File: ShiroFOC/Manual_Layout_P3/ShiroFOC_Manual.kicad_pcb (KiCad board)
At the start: 6 copper layers, 45 x 45 mm, 279 parts, among them J1 Motor phases - solder wires, J1001 TC2030-NL SWD, J101 DC input - solder wires, J201 USB-C service, J501 BRAKE RESISTOR, J502 5V PWM FAN, J601 EXT ENCODER / HALL, J801 CAN 1, J802 CAN 2, Q201 CSD17483F4, Q301 CSD17483F4, Q501 ISZ080N10NM6 100V, Q801 CSD17483F4, Q802 CSD87502Q2, SW301 RESET, U1 CSD88599Q5DC, U2 CSD88599Q5DC, U201 LMR36510FADDAR, U202 USBLC6-2SC6, U203 TPS2121RUXR, U204 TLV75533PDYDR, U205 MPM3620AGQV-Z, U3 CSD88599Q5DC, U4 STSPIN32G4, U501 UCC27517ADBVR, U502 TLV3012BIDCKR, U503 74AHCT1G125W5-7, U601 AS5047P-ATSM, U602 TMUX1574PW, U603 74LVC3G17, U604 TPS2553DBVR, U701 BMI323, U801 TCAN3413DRBR, U901 CP2102N-A02-GQFN20, Y301 24MHz 7pF

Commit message: Routing started
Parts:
- removed C107: RC DAMP C - TUNE, Capacitor_SMD:C_2220_5750Metric
- removed C125, C126, C142, C143, C159, C160: 10uF DNP, Capacitor_SMD:C_1210_3225Metric
- removed C413, C423, C433: TUNE DNP, Capacitor_SMD:C_1206_3216Metric
- removed D101: VM TVS - SELECT AFTER TEST, Diode_SMD:D_SMC
- removed R102: RC DAMP R - TUNE, Resistor_SMD:R_2512_6332Metric
- removed R303: 2k2, Resistor_SMD:R_0402_1005Metric
- removed R415, R425, R435: TUNE DNP, Resistor_SMD:R_1206_3216Metric
- removed SW301: RESET, Button_Switch_SMD:SW_Push_1P1T-SH_NO_CK_KMR2xxG
- C506, C605, C607, C701, C702, R101, R307, R308, U503, U701: moved to B.Cu
- R313, R314: moved to F.Cu
- moved C702 78.8 mm to (-3.90, -5.90)
- moved C701 78.8 mm to (-3.90, -4.02)
- moved J1001 76.4 mm to (12.1, 20.5), turned to 180 degrees
- moved U701 75.0 mm to (-6.01, -4.96)
- moved R308 73.5 mm to (-8.59, -4.71)
- moved TH701 73.3 mm to (-13.5, 36.8)
- moved R715 73.3 mm to (-8.59, -5.70)
- moved C106 70.0 mm to (11.0, -8.17), turned to 90 degrees
- moved C105 68.1 mm to (12.0, -8.17), turned to 90 degrees
- moved TH702 62.4 mm to (-14.4, 41.4)
- moved TH703 59.3 mm to (-13.1, 52.0)
- moved R101 57.3 mm to (25.3, -9.53), turned to 90 degrees
- moved C607 54.3 mm to (-1.57, 18.1), turned to 180 degrees
- moved C603 50.6 mm to (-7.27, 16.2), turned to 180 degrees
- moved C605 49.0 mm to (-13.1, 16.7), turned to 180 degrees
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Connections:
- U602 pad 4: FEEDBACK_A_H1 -> FEEDBACK_B_H2
- U602 pad 7: FEEDBACK_B_H2 -> FEEDBACK_A_H1
- U603 pad 5: Net-(U602A-S2B) -> Net-(U602A-S1B)
- U603 pad 7: Net-(U602A-S1B) -> Net-(U602A-S2B)
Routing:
- net GND: track 19.4 -> 54.5 mm, vias 12 -> 15
- net VM: track 18.1 -> 52.3 mm
- net 3V3: track 19.9 -> 36.0 mm, vias 6 -> 5
- net GLS3: track 18.8 -> 6.56 mm, vias 3 -> 2
- net Net-(R103-Pad2): track 0.00 -> 8.31 mm, vias 0 -> 2
- net GLS2: track 16.2 -> 7.98 mm
- net EXT_VCC: track 0.00 -> 8.06 mm, vias 0 -> 1
- net Net-(U601-MOSI): track 0.00 -> 7.37 mm, vias 0 -> 1
- net Net-(U602A-S1B): track 0.00 -> 5.40 mm
- net PHASE_U: track 0.00 -> 4.78 mm
- net PHASE_V: track 0.00 -> 4.30 mm
- net Net-(U602A-S2B): track 0.00 -> 4.15 mm
- net Net-(U503-A): track 0.00 -> 4.06 mm
- net SPI3_MOSI_MCU: track 0.00 -> 3.81 mm
- net GLS1: track 19.3 -> 15.7 mm
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- added copper zone on F.Cu, net /Three-phase bridge/LS_SOURCE_U
- added copper zone on F.Cu, net /Three-phase bridge/LS_SOURCE_V
- added copper zone on F.Cu, net /Three-phase bridge/LS_SOURCE_W
- added copper zone on F.Cu, net GND
- added copper zone on F.Cu, net PHASE_U
- added copper zone on F.Cu, net PHASE_V
- added copper zone on F.Cu, net PHASE_W
- added copper zone on F.Cu, net VM
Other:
- board text removed: "10 V AUXILIARY POWER"
- board text removed: "5 V / POWER MUX / 3.3 V"
- board text removed: "50 x 50 mm"
- board text removed: "55 x 55 mm"
- board text removed: "60 x 60 mm"
- board text removed: "70 x 70 mm"
- board text removed: "80 x 80 mm"
- board text removed: "BRAKE CHOPPER"
- board text removed: "BRAKE NTC"
- board text removed: "BRIDGE ROUTING - FIXED"
- board text removed: "CAN INTERFACE"
- board text removed: "DC INPUT"
- board text removed: "DC LINK / BULK CAPACITORS"
- board text removed: "DC LINK PROTECTION / DAMPING"
- board text removed: "ENCODER - CENTRED AS5047"
- board text removed: "EXTERNAL ENCODER / HALL"
- board text removed: "FEEDBACK MUX / BUS SENSE"
- board text removed: "HALF-BRIDGES / SHUNTS - FIXED"
- board text removed: "IMU"
- board text removed: "MCU + ANALOG - FIXED"
- board text removed: "MCU / OP-AMP R + C - FIXED"
- board text removed: "RESET / STATUS"
- board text removed: "SWD"
- board text removed: "TEMPERATURE / ADC FILTERS"
- board text removed: "USB / UART"

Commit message: most caps placed
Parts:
- removed C148, C150, C153, C155, C157: 10uF, Capacitor_SMD:C_1210_3225Metric
- removed R313, R314: 22R, Resistor_SMD:R_0402_1005Metric
- removed R611: 33R, Resistor_SMD:R_0402_1005Metric
- C101, C102, C103, C105, C106, C11, C110, C111, C112, C113, C114, C115, C116, C117, C118, C119, C120, C121, C123, C124, C127, C128, C129, C130, C134, C135, C136, C137, C139, C144, C145, C146, C147, C149, C154, C156, C158, C3, C7: moved to B.Cu
- C701, C702, R103, R308, R715, R903, U701: moved to F.Cu
- moved C147 100.2 mm to (5.55, 17.1), turned to 180 degrees
- moved C146 97.6 mm to (5.55, 7.40), turned to 180 degrees
- moved C156 95.8 mm to (5.55, -4.16), turned to 180 degrees
- moved C158 95.8 mm to (5.55, 4.15), turned to 180 degrees
- moved C154 93.4 mm to (10.2, -5.60), turned to 180 degrees
- moved C140 93.1 mm to (7.34, 20.0), turned to -90 degrees
- moved C130 89.3 mm to (5.55, 10.7), turned to 180 degrees
- moved C141 88.1 mm to (10.6, 20.0), turned to -90 degrees
- moved C139 87.1 mm to (6.25, 0.20), turned to 90 degrees
- moved C152 84.8 mm to (13.8, 20.0), turned to -90 degrees
- moved C151 83.4 mm to (9.81, -6.72), turned to 90 degrees
- moved C136 78.9 mm to (2.56, -8.55), turned to 180 degrees
- moved C149 77.6 mm to (15.5, -16.4), turned to -90 degrees
- moved C144 76.4 mm to (14.8, 13.9)
- moved C133 74.8 mm to (6.73, -20.0), turned to -90 degrees
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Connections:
- U601 pad 2: Net-(U601-CLK) -> SPI3_SCK_MCU
- U601 pad 3: Net-(U601-MISO) -> SPI3_MISO
- U601 pad 4: Net-(U601-MOSI) -> SPI3_MOSI_MCU
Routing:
- net VM: track 52.3 -> 99.9 mm
- net GHS2: track 19.0 -> 60.5 mm
- net FDCAN1_RX: track 0.00 -> 31.5 mm, vias 1 -> 2
- net FDCAN1_TX: track 1.35 -> 29.0 mm, vias 1 -> 2
- net USB_UART_RX: track 0.00 -> 26.5 mm, vias 1 -> 2
- net /USB service/UART_BRIDGE_RX: track 4.90 -> 30.0 mm, vias 1 -> 2
- net I2C2_SCL: track 1.16 -> 15.9 mm, vias 1 -> 2
- net SHUNT_U_SENSE_P: track 25.0 -> 10.4 mm
- net /MCU / clock / SWD/SWCLK: track 0.00 -> 13.6 mm, vias 0 -> 2
- net AS5047P_CS_N: track 0.00 -> 13.4 mm, vias 0 -> 2
- net SHUNT_U_SENSE_N: track 24.7 -> 11.4 mm
- net I2C2_SDA: track 1.16 -> 13.5 mm, vias 1 -> 2
- net SPI3_MISO: track 0.00 -> 10.9 mm, vias 0 -> 1
- net GND: track 54.5 -> 65.0 mm, vias 15 -> 13
- net HS_RETURN_U: track 21.0 -> 10.8 mm
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
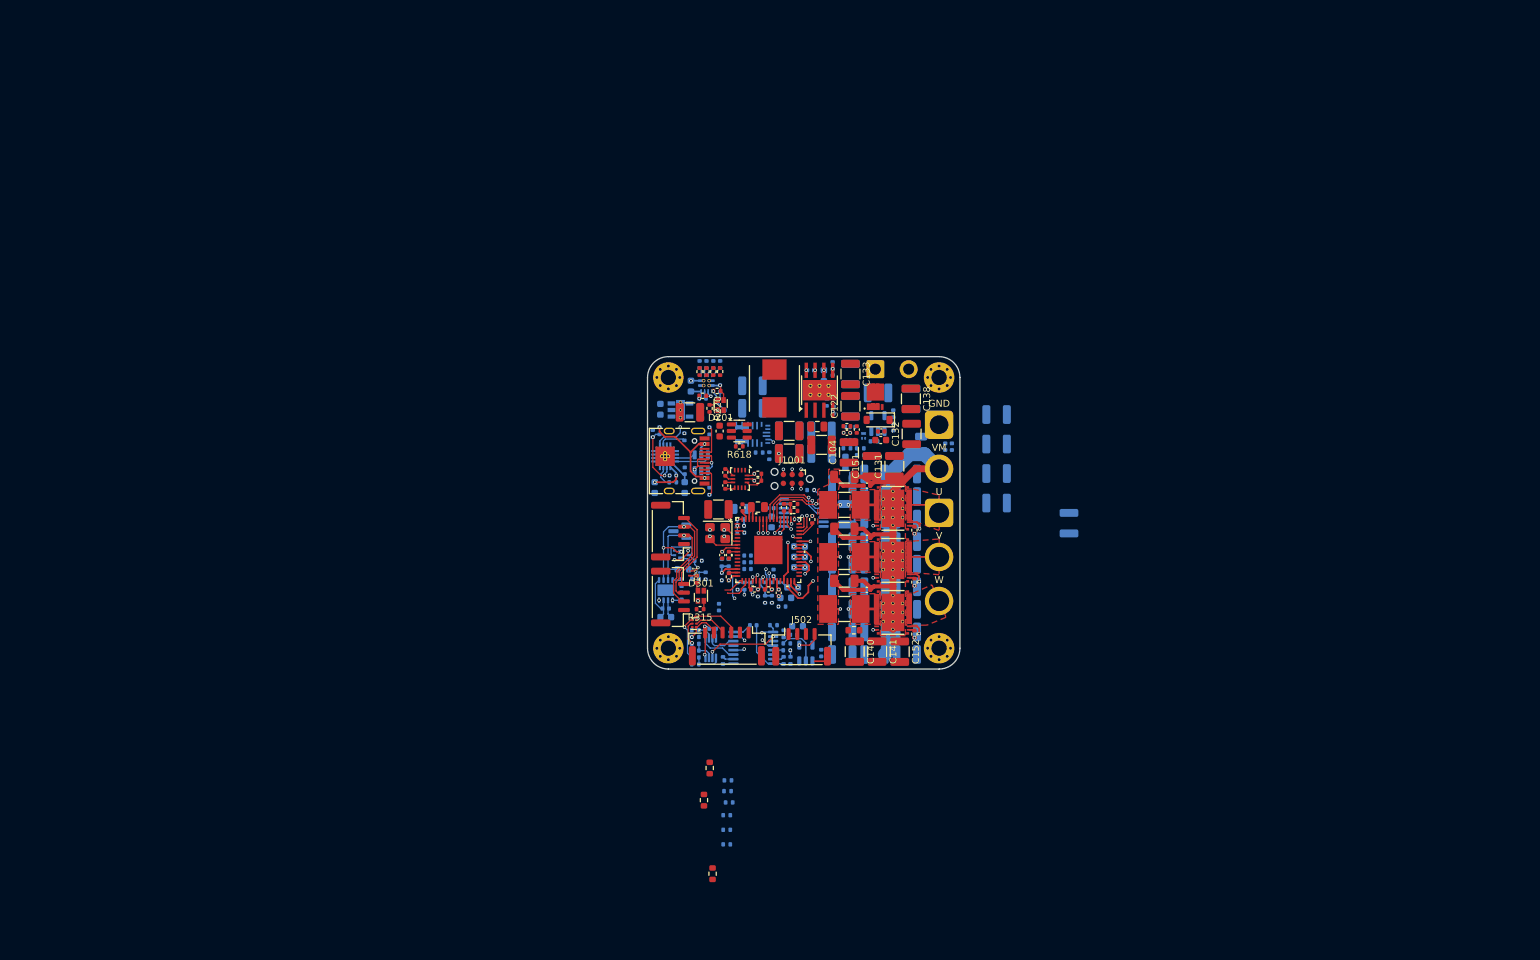
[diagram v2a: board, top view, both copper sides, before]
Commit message: can connector rewiring
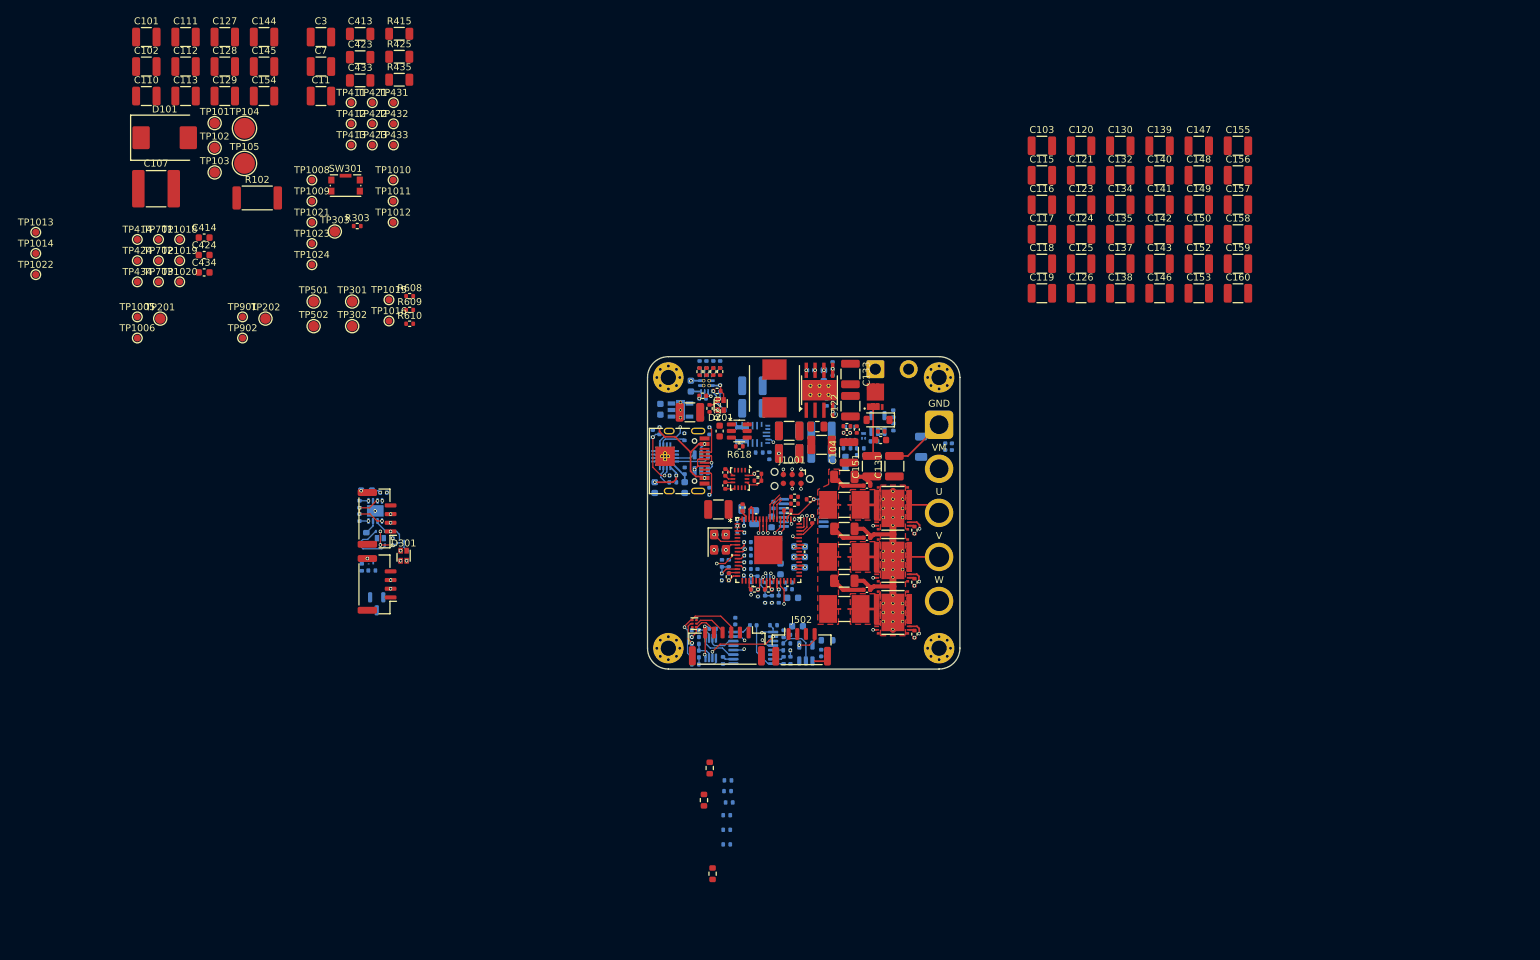
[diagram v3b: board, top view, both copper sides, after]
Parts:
- added C107: RC DAMP C - TUNE, Capacitor_SMD:C_2220_5750Metric, F.Cu at (-93.3, -46.7)
- added C125: 10uF DNP, Capacitor_SMD:C_1210_3225Metric, F.Cu at (40.0, -35.9)
- added C126: 10uF DNP, Capacitor_SMD:C_1210_3225Metric, F.Cu at (40.0, -31.6)
- added C142: 10uF DNP, Capacitor_SMD:C_1210_3225Metric, F.Cu at (51.3, -40.1)
- added C143: 10uF DNP, Capacitor_SMD:C_1210_3225Metric, F.Cu at (51.3, -35.9)
- added C148: 10uF, Capacitor_SMD:C_1210_3225Metric, F.Cu at (56.9, -48.6)
- added C150: 10uF, Capacitor_SMD:C_1210_3225Metric, F.Cu at (56.9, -40.1)
- added C153: 10uF, Capacitor_SMD:C_1210_3225Metric, F.Cu at (56.9, -31.6)
- added C155: 10uF, Capacitor_SMD:C_1210_3225Metric, F.Cu at (62.6, -52.9)
- added C157: 10uF, Capacitor_SMD:C_1210_3225Metric, F.Cu at (62.6, -44.4)
- added C159: 10uF DNP, Capacitor_SMD:C_1210_3225Metric, F.Cu at (62.6, -35.9)
- added C160: 10uF DNP, Capacitor_SMD:C_1210_3225Metric, F.Cu at (62.6, -31.6)
- added C413: TUNE DNP, Capacitor_SMD:C_1206_3216Metric, F.Cu at (-63.9, -69.0)
- added C414: 47pF C0G, Capacitor_SMD:C_0603_1608Metric, F.Cu at (-86.4, -39.6)
- added C423: TUNE DNP, Capacitor_SMD:C_1206_3216Metric, F.Cu at (-63.9, -65.6)
- added C424: 47pF C0G, Capacitor_SMD:C_0603_1608Metric, F.Cu at (-86.4, -37.1)
- added C433: TUNE DNP, Capacitor_SMD:C_1206_3216Metric, F.Cu at (-63.9, -62.3)
- added C434: 47pF C0G, Capacitor_SMD:C_0603_1608Metric, F.Cu at (-86.4, -34.6)
- added D101: VM TVS - SELECT AFTER TEST, Diode_SMD:D_SMC, F.Cu at (-92.0, -54.0)
- added R102: RC DAMP R - TUNE, Resistor_SMD:R_2512_6332Metric, F.Cu at (-78.7, -45.4)
- added R303: 2k2, Resistor_SMD:R_0402_1005Metric, F.Cu at (-64.3, -41.3)
- added R415: TUNE DNP, Resistor_SMD:R_1206_3216Metric, F.Cu at (-58.3, -69.0)
- added R425: TUNE DNP, Resistor_SMD:R_1206_3216Metric, F.Cu at (-58.3, -65.7)
- added R435: TUNE DNP, Resistor_SMD:R_1206_3216Metric, F.Cu at (-58.3, -62.4)
- added R608: 4.7k DNP, Resistor_SMD:R_0402_1005Metric, F.Cu at (-56.8, -31.2)
- added R609: 4.7k DNP, Resistor_SMD:R_0402_1005Metric, F.Cu at (-56.8, -29.2)
- added R610: 4.7k DNP, Resistor_SMD:R_0402_1005Metric, F.Cu at (-56.8, -27.2)
- added SW301: RESET, Button_Switch_SMD:SW_Push_1P1T-SH_NO_CK_KMR2xxG, F.Cu at (-66.0, -47.1)
- added TP1005: 5V_SYS, TestPoint:TestPoint_Pad_D1.0mm, F.Cu at (-96.0, -28.2)
- added TP1006: 3V3, TestPoint:TestPoint_Pad_D1.0mm, F.Cu at (-96.0, -25.2)
- added TP1008: SWDIO, TestPoint:TestPoint_Pad_D1.0mm, F.Cu at (-70.8, -47.9)
- added TP1009: SWCLK, TestPoint:TestPoint_Pad_D1.0mm, F.Cu at (-70.8, -44.9)
- added TP101: VM, TestPoint:TestPoint_Pad_D1.5mm, F.Cu at (-84.9, -56.1)
- added TP1010: ENC_SPI_CLK, TestPoint:TestPoint_Pad_D1.0mm, F.Cu at (-59.1, -47.9)
- added TP1011: SPI3_MISO, TestPoint:TestPoint_Pad_D1.0mm, F.Cu at (-59.1, -44.9)
- added TP1012: ENC_SPI_MOSI, TestPoint:TestPoint_Pad_D1.0mm, F.Cu at (-59.1, -41.8)
- added TP1013: FDCAN1_TX, TestPoint:TestPoint_Pad_D1.0mm, F.Cu at (-110.6, -40.4)
- added TP1014: FDCAN1_RX, TestPoint:TestPoint_Pad_D1.0mm, F.Cu at (-110.6, -37.4)
- added TP1015: FEEDBACK_A_H1, TestPoint:TestPoint_Pad_D1.0mm, F.Cu at (-59.7, -30.7)
- added TP1016: FEEDBACK_B_H2, TestPoint:TestPoint_Pad_D1.0mm, F.Cu at (-59.7, -27.6)
- added TP1018: OPO_U1, TestPoint:TestPoint_Pad_D1.0mm, F.Cu at (-89.9, -39.4)
- added TP1019: OPO_V1, TestPoint:TestPoint_Pad_D1.0mm, F.Cu at (-89.9, -36.3)
- added TP102: GND, TestPoint:TestPoint_Pad_D1.5mm, F.Cu at (-84.9, -52.6)
- added TP1020: OPO_W1, TestPoint:TestPoint_Pad_D1.0mm, F.Cu at (-89.9, -33.3)
- added TP1021: CAN_TERM_DISABLE, TestPoint:TestPoint_Pad_D1.0mm, F.Cu at (-70.8, -41.8)
- added TP1022: CAN_STB, TestPoint:TestPoint_Pad_D1.0mm, F.Cu at (-110.6, -34.3)
- added TP1023: EXT_POWER_FAULT_N, TestPoint:TestPoint_Pad_D1.0mm, F.Cu at (-70.8, -38.8)
- added TP1024: I2C2_SDA, TestPoint:TestPoint_Pad_D1.0mm, F.Cu at (-70.8, -35.7)
- added TP103: VBUS_SENSE, TestPoint:TestPoint_Pad_D1.5mm, F.Cu at (-84.9, -49.0)
- added TP104: VM BULK, TestPoint:TestPoint_Pad_D3.0mm, F.Cu at (-80.6, -55.4)
- added TP105: GND BULK, TestPoint:TestPoint_Pad_D3.0mm, F.Cu at (-80.6, -50.3)
- added TP201: PWR_SOURCE_STATUS, TestPoint:TestPoint_Pad_D1.5mm, F.Cu at (-92.7, -28.0)
- added TP202: 5V_USB, TestPoint:TestPoint_Pad_D1.5mm, F.Cu at (-77.5, -28.0)
- added TP301: VCC, TestPoint:TestPoint_Pad_D1.5mm, F.Cu at (-65.0, -30.4)
- added TP302: SCREF, TestPoint:TestPoint_Pad_D1.5mm, F.Cu at (-65.0, -26.9)
- added TP303: NRST, TestPoint:TestPoint_Pad_D1.5mm, F.Cu at (-67.5, -40.5)
- added TP411: GL, TestPoint:TestPoint_Pad_D1.0mm, F.Cu at (-65.2, -59.1)
- added TP412: SOURCE, TestPoint:TestPoint_Pad_D1.0mm, F.Cu at (-65.2, -56.0)
- added TP413: PHASE, TestPoint:TestPoint_Pad_D1.0mm, F.Cu at (-65.2, -53.0)
- added TP414: SCOPE GND, TestPoint:TestPoint_Pad_D1.0mm, F.Cu at (-96.0, -39.4)
- added TP421: GL, TestPoint:TestPoint_Pad_D1.0mm, F.Cu at (-62.1, -59.1)
- added TP422: SOURCE, TestPoint:TestPoint_Pad_D1.0mm, F.Cu at (-62.1, -56.0)
- added TP423: PHASE, TestPoint:TestPoint_Pad_D1.0mm, F.Cu at (-62.1, -53.0)
- added TP424: SCOPE GND, TestPoint:TestPoint_Pad_D1.0mm, F.Cu at (-96.0, -36.3)
- added TP431: GL, TestPoint:TestPoint_Pad_D1.0mm, F.Cu at (-59.1, -59.1)
- added TP432: SOURCE, TestPoint:TestPoint_Pad_D1.0mm, F.Cu at (-59.1, -56.0)
- added TP433: PHASE, TestPoint:TestPoint_Pad_D1.0mm, F.Cu at (-59.1, -53.0)
- added TP434: SCOPE GND, TestPoint:TestPoint_Pad_D1.0mm, F.Cu at (-96.0, -33.3)
- added TP501: BRAKE_GATE, TestPoint:TestPoint_Pad_D1.5mm, F.Cu at (-70.6, -30.4)
- added TP502: BRAKE_SWITCH, TestPoint:TestPoint_Pad_D1.5mm, F.Cu at (-70.6, -26.9)
- added TP701: NTC_PHASE_A, TestPoint:TestPoint_Pad_D1.0mm, F.Cu at (-92.9, -39.4)
- added TP702: NTC_PHASE_B, TestPoint:TestPoint_Pad_D1.0mm, F.Cu at (-92.9, -36.3)
- added TP703: NTC_PHASE_C, TestPoint:TestPoint_Pad_D1.0mm, F.Cu at (-92.9, -33.3)
- added TP901: USB_UART_TX, TestPoint:TestPoint_Pad_D1.0mm, F.Cu at (-80.8, -28.2)
- added TP902: USB_UART_RX, TestPoint:TestPoint_Pad_D1.0mm, F.Cu at (-80.8, -25.2)
- C101, C102, C103, C11, C110, C111, C112, C113, C115, C116, C117, C118, C119, C120, C121, C123, C124, C127, C128, C129, C130, C134, C135, C137, C139, C144, C145, C146, C147, C149, C154, C156, C158, C3, C7, R309: moved to F.Cu
- C108, C303, C310, C311, Q301, R103, R304, R315: moved to B.Cu
- moved C101 129.7 mm to (-94.7, -68.5)
- moved C102 128.9 mm to (-94.7, -64.3), turned to 0 degrees
- moved C110 128.6 mm to (-94.7, -60.0)
- moved C129 124.9 mm to (-83.4, -60.0)
- moved C128 124.1 mm to (-83.4, -64.3), turned to 0 degrees
- moved C144 124.0 mm to (-77.7, -68.5)
- moved C111 123.2 mm to (-89.0, -68.5)
- moved C113 122.1 mm to (-89.0, -60.0)
- moved C145 119.1 mm to (-77.7, -64.3)
- moved C127 118.5 mm to (-83.4, -68.5), turned to 0 degrees
- moved C112 117.0 mm to (-89.0, -64.3), turned to 0 degrees
- moved C11 108.7 mm to (-69.5, -60.0), turned to 0 degrees
- moved C7 107.2 mm to (-69.5, -64.3), turned to 0 degrees
- moved C3 105.7 mm to (-69.5, -68.5), turned to 0 degrees
- moved C154 103.4 mm to (-77.7, -60.0), turned to 0 degrees
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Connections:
- D801 pad 1: /CAN interface/CANL_BUS -> /CAN interface/CANH_BUS
- D801 pad 2: /CAN interface/CANH_BUS -> /CAN interface/CANL_BUS
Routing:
- net GHS2: track 60.5 -> 0.00 mm, vias 2 -> 1
- net VM: track 99.9 -> 57.4 mm
- net FDCAN1_RX: track 31.5 -> 6.47 mm
- net FDCAN1_TX: track 29.0 -> 7.80 mm
- net HS_RETURN_V: track 21.2 -> 3.23 mm
- net GHS3: track 17.4 -> 0.00 mm, vias 2 -> 1
- net SHUNT_W_SENSE_P: track 18.5 -> 1.49 mm, vias 2 -> 1
- net HS_RETURN_W: track 19.1 -> 3.23 mm
- net USB_UART_RX: track 26.5 -> 10.6 mm
- net I2C2_SCL: track 15.9 -> 0.00 mm, vias 2 -> 0
- net /USB service/UART_BRIDGE_RX: track 30.0 -> 14.2 mm
- net GLS1: track 15.7 -> 0.50 mm, vias 2 -> 1
- net /CAN interface/CANL_BUS: track 25.8 -> 12.1 mm, vias 3 -> 2
- net /MCU / clock / SWD/SWCLK: track 13.6 -> 1.50 mm
- net /CAN interface/CAN_SHIELD: track 11.5 -> 0.00 mm
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- removed copper zone on F.Cu, net PHASE_U
- removed copper zone on F.Cu, net PHASE_V
- removed copper zone on F.Cu, net PHASE_W
